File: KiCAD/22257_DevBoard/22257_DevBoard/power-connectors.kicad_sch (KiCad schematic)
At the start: 10 parts, among them U3 TPS73633DBV

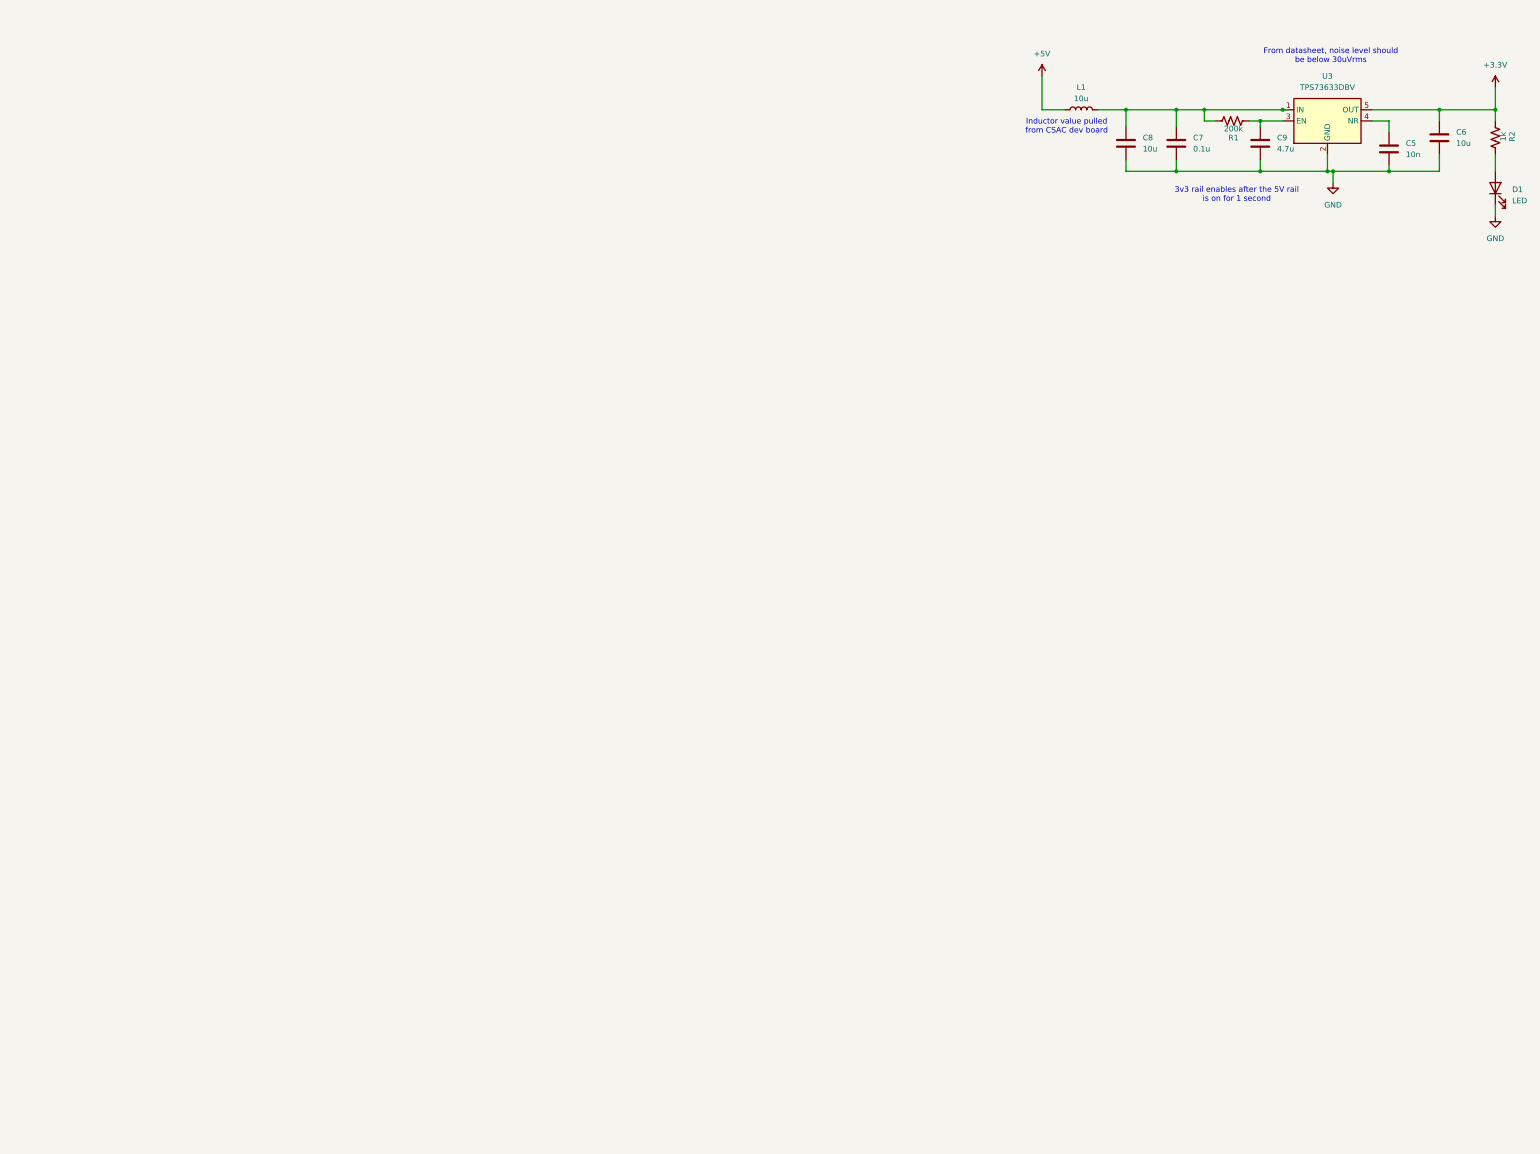
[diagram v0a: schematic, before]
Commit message: More Schematic Updates
Added power monitors and connectors, along with finishing the power circuitry.
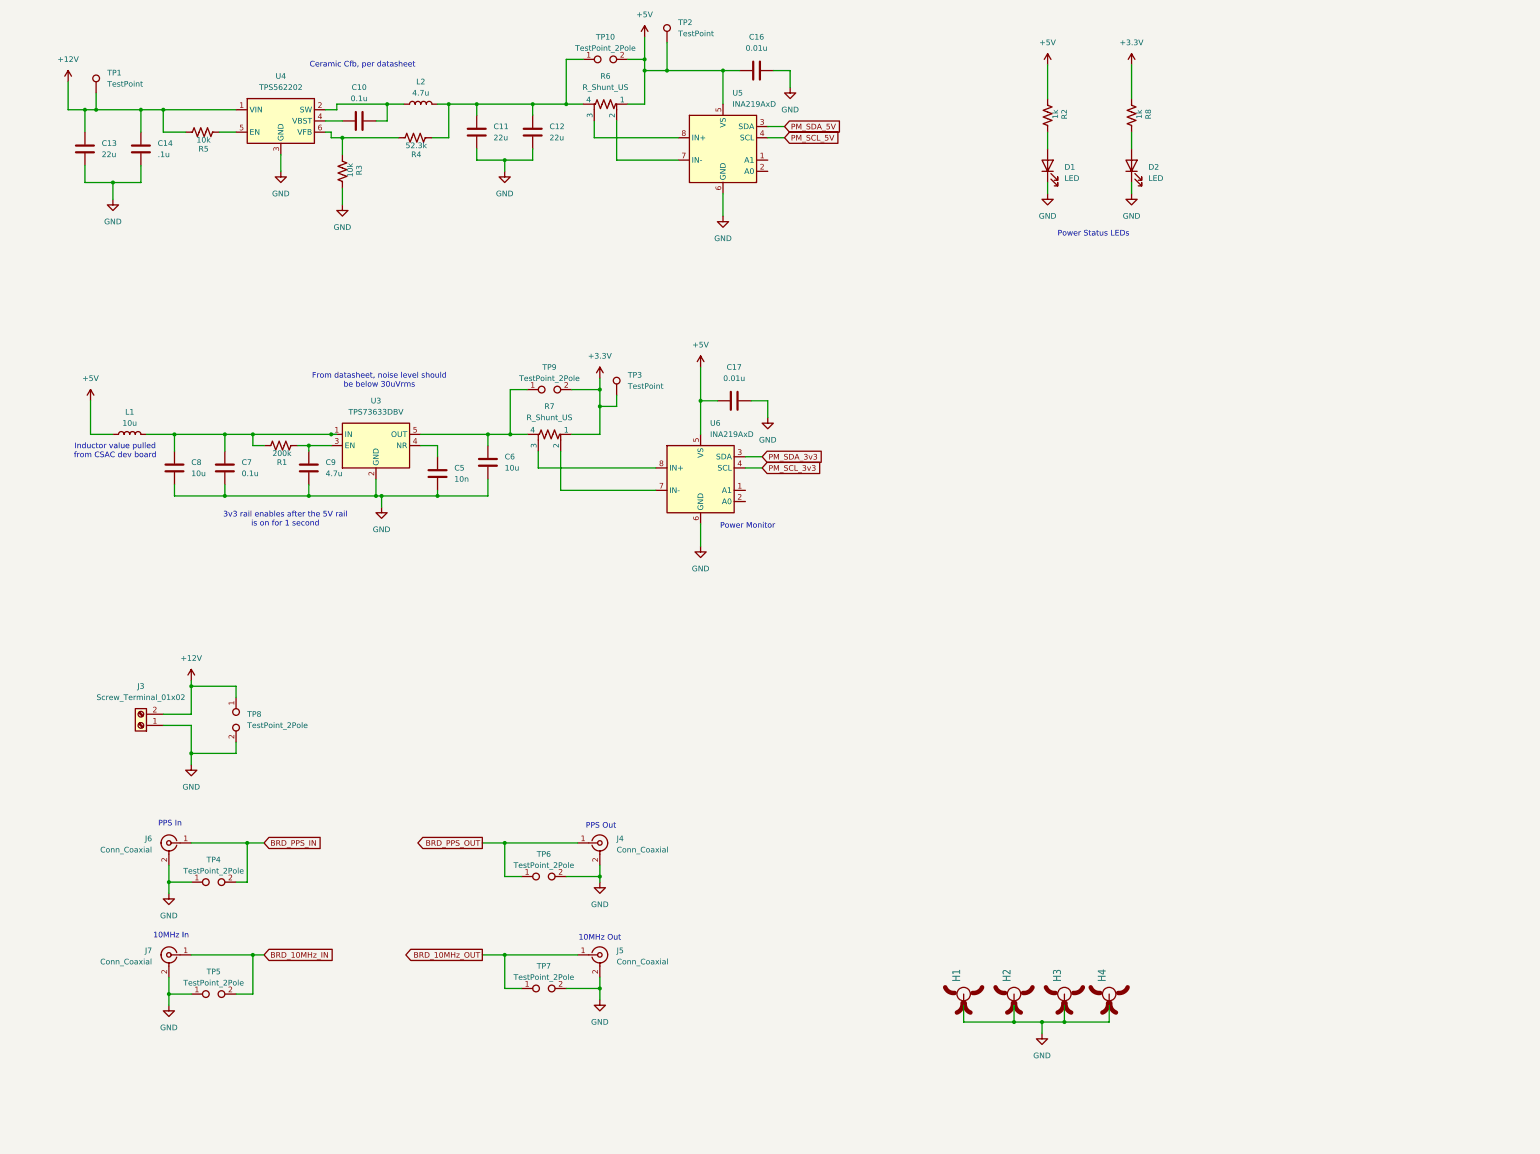
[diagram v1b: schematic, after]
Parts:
- added C10: 0.1u, symbol Device:C
- added C11, C12, C13: 22u, symbol Device:C
- added C14: .1u, symbol Device:C
- added C16, C17: 0.01u, symbol Device:C
- added D2: LED, symbol Device:LED
- added H1, H2, H3, H4: MOUNT-PAD-ROUND5.0, ZED_BREAKOUT_v22:5,0-PAD, symbol ZED_BREAKOUT_v22-eagle-import:MOUNT-PAD-ROUND5.0
- added J3: Screw_Terminal_01x02, symbol Connector:Screw_Terminal_01x02
- added J4, J5, J6, J7: Conn_Coaxial, symbol Connector:Conn_Coaxial
- added L2: 4.7u, symbol Device:L
- added R3, R5: 10k, symbol Device:R_US
- added R4: 52.3k, symbol Device:R_US
- added R6, R7: R_Shunt_US, symbol Device:R_Shunt_US
- added R8: 1k, symbol Device:R_US
- added TP1, TP2, TP3: TestPoint, symbol Connector:TestPoint
- added TP10, TP4, TP5, TP6, TP7, TP8, TP9: TestPoint_2Pole, symbol Connector:TestPoint_2Pole
- added U4: TPS562202, Package_TO_SOT_SMD:SOT-563, symbol Regulator_Switching:TPS562202
- added U5, U6: INA219AxD, Package_SO:SOIC-8_3.9x4.9mm_P1.27mm, symbol Sensor_Energy:INA219AxD
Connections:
- net +3.3V: now also R7.1, R8.2, TP3.1, TP9.2; no longer C6.1, R2.2, U3.5 (OUT)
- net +5V: now also R2.2, C16.1, C17.1, R6.1, TP10.2, TP2.1, U5.5 (VS), U6.5 (VS)
- net GND: now also C11.1, C12.1, C13.1, C14.1, C16.2, C17.2, D2.1 (K), H1.B5 (MOUNT), H2.B5 (MOUNT), H3.B5 (MOUNT), H4.B5 (MOUNT), J3.1 (Pin_1), J4.2 (Ext), J5.2 (Ext), J6.2 (Ext), J7.2 (Ext), R3.1, TP4.1, TP5.1, TP6.2, TP7.2, TP8.2, U4.3 (GND), U5.6 (GND), U6.6 (GND)
- new net: R7.2, U6.7 (IN-)
- new net: R7.3, U6.8 (IN+)
- new net: C6.1, R7.4, TP9.1, U3.5 (OUT)
- new net: R3.2, R4.1, U4.6 (VFB)
- new net: C11.2, C12.2, L2.2, R4.2, R6.4, TP10.1
- new net: R6.2, U5.7 (IN-)
- new net: R6.3, U5.8 (IN+)
- new net: C10.2, L2.1, U4.2 (SW)
- new net: C10.1, U4.4 (VBST)
- new net: R5.2, U4.5 (EN)
- new net: D2.2 (A), R8.1
- new net +12V: C13.2, C14.2, J3.2 (Pin_2), R5.1, TP1.1, TP8.1, U4.1 (VIN)
- new net BRD_10MHz_IN: J7.1 (In), TP5.2
- new net BRD_10MHz_OUT: J5.1 (In), TP7.1
- new net BRD_PPS_IN: J6.1 (In), TP4.2
- new net BRD_PPS_OUT: J4.1 (In), TP6.1
- new net PM_SCL_3v3: U6.4 (SCL)
- new net PM_SCL_5V: U5.4 (SCL)
- new net PM_SDA_3v3: U6.3 (SDA)
- new net PM_SDA_5V: U5.3 (SDA)
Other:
- note added: "10MHz In"
- note added: "10MHz Out"
- note added: "Ceramic Cfb, per datasheet"
- note added: "PPS In"
- note added: "PPS Out"
- note added: "Power Monitor"
- note added: "Power Status LEDs"
- moved on the sheet: C5, C6, C7, C8, C9, D1, L1, R1, R2, U3

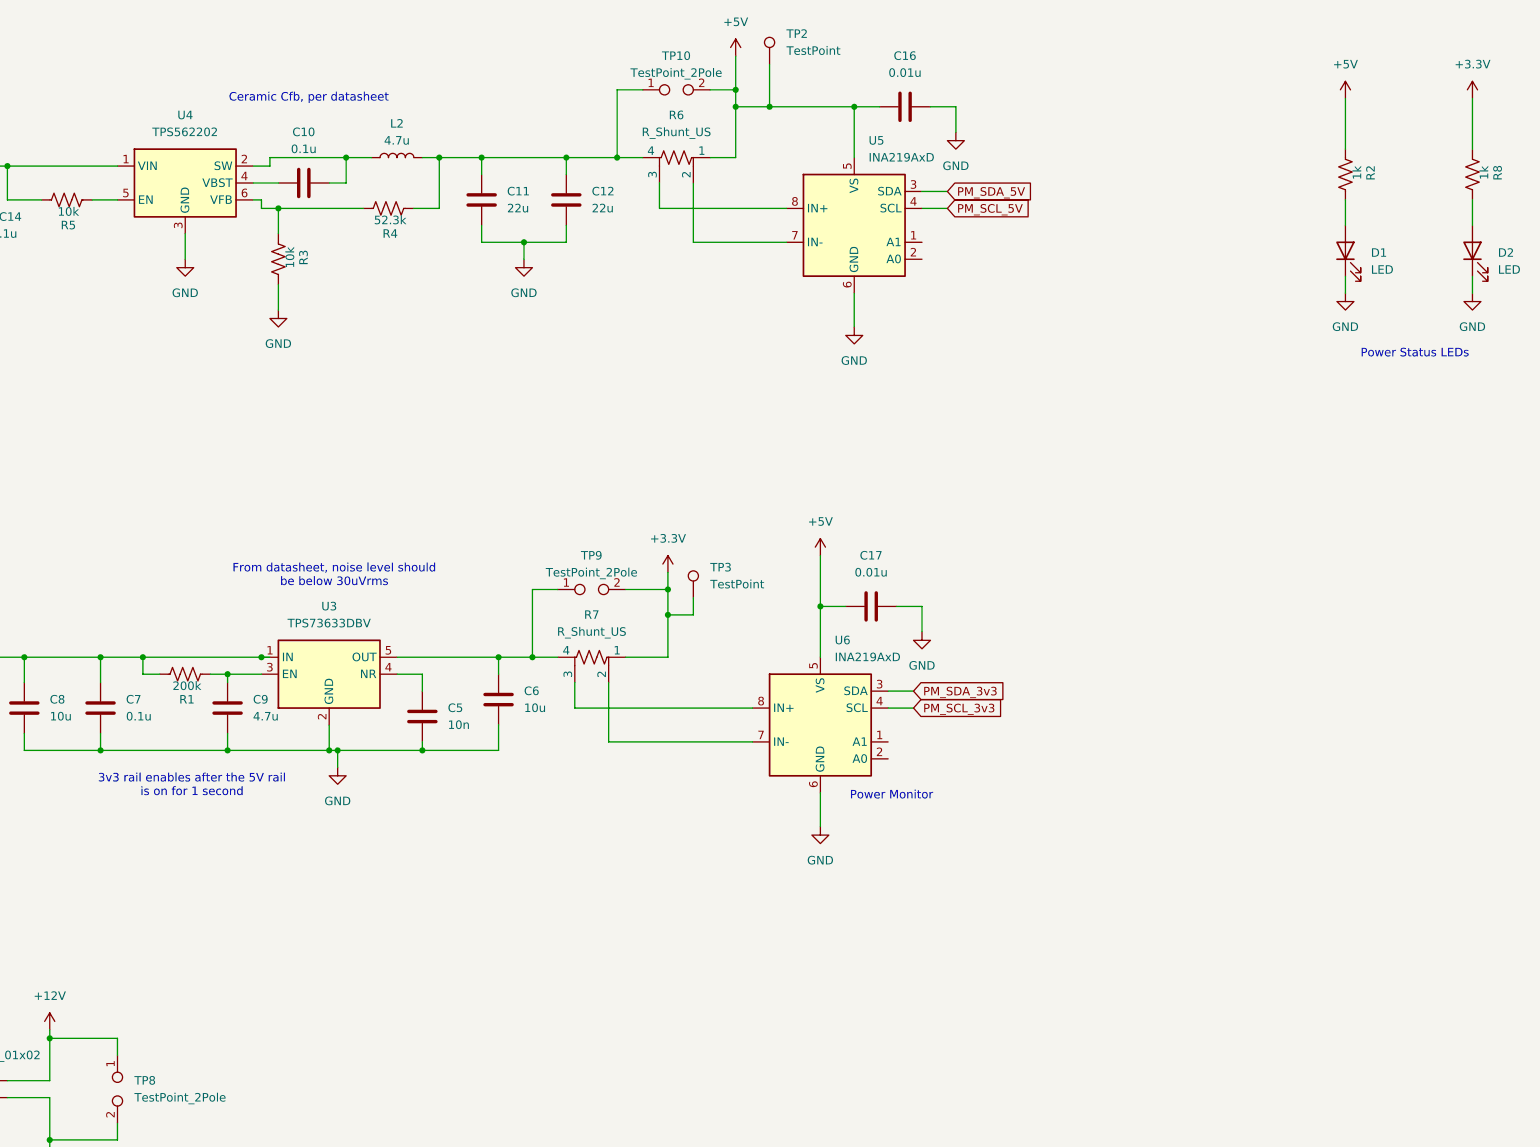
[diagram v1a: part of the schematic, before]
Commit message: Schematic should be finished, onto layout
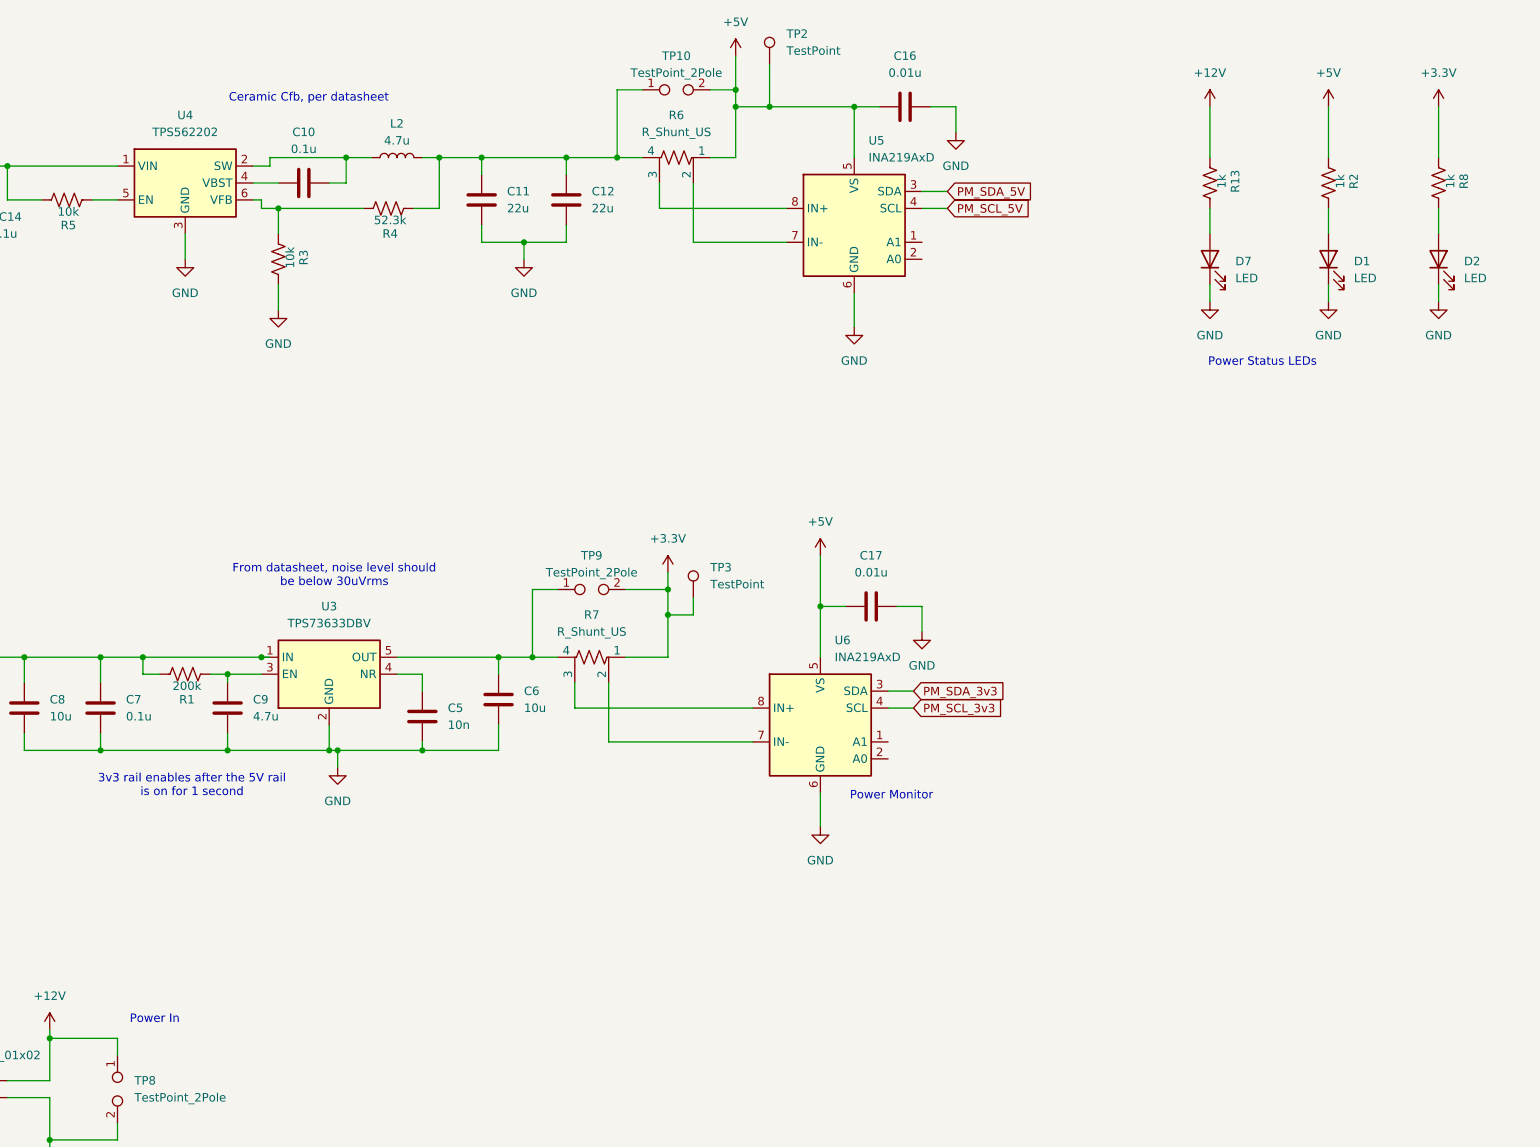
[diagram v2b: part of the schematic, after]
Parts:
- added D7: LED, symbol Device:LED
- added R13: 1k, symbol Device:R_US
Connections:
- net +12V: now also R13.2
- net GND: now also D7.1 (K)
- new net: D7.2 (A), R13.1
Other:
- note added: "Power In"
- moved on the sheet: D1, D2, R2, R8

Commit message: Assignmed Most footprints. Created footprints for oscillators.
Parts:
- C10, C11, C12, C13, C14, C16, C17, C5, C6, C7, C8, C9: footprint (none) -> Capacitor_SMD:C_0603_1608Metric
- D1, D2, D7: footprint (none) -> LED_SMD:LED_0603_1608Metric
- J3: footprint (none) -> Connector_Phoenix_GMSTB:PhoenixContact_GMSTBA_2,5_2-G-7,62_1x02_P7.62mm_Horizontal
- J4, J5, J6, J7: footprint (none) -> Connector_Coaxial:SMA_Amphenol_901-143_Horizontal
- R1, R2, R3, R4, R5: footprint (none) -> Resistor_SMD:R_0603_1608Metric
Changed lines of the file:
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@@
 			)
 		)
-		(property "Footprint" ""
+		(property "Footprint" "Capacitor_SMD:C_0603_1608Metric"
 			(at 120.3452 132.08 0)
 			(effects
@@
 			)
 		)
-		(property "Footprint" ""
+		(property "Footprint" "Capacitor_SMD:C_0603_1608Metric"
 			(at 190.5 110.7948 0)
 			(effects
@@
 			)
 		)
-		(property "Footprint" ""
+		(property "Footprint" "Capacitor_SMD:C_0603_1608Metric"
 			(at 195.58 35.8648 0)
 			(effects
@@
 			)
 		)
-		(property "Footprint" ""
+		(property "Footprint" "Resistor_SMD:R_0603_1608Metric"
 			(at 114.554 51.054 90)
 			(effects
@@
 			)
 		)
-		(property "Footprint" ""
+		(property "Footprint" "Resistor_SMD:R_0603_1608Metric"
 			(at 96.774 59.436 90)
 			(effects
@@
 			)
 		)
-		(property "Footprint" ""
+		(property "Footprint" "LED_SMD:LED_0603_1608Metric"
 			(at 255.27 59.69 0)
 			(effects
@@
 			)
 		)
-		(property "Footprint" ""
+		(property "Footprint" "Connector_Phoenix_GMSTB:PhoenixContact_GMSTBA_2,5_2-G-7,62_1x02_P7.62mm_Horizontal"
 			(at 52.07 185.42 0)
 			(effects
@@
 			)
 		)
-		(property "Footprint" ""
+		(property "Footprint" "Capacitor_SMD:C_0603_1608Metric"
 			(at 131.7752 129.54 0)
 			(effects
@@
 			)
 		)
-		(property "Footprint" ""
+		(property "Footprint" "Capacitor_SMD:C_0603_1608Metric"
 			(at 51.1048 50.8 0)
 			(effects
@@
 			)
 		)
-		(property "Footprint" ""
+		(property "Footprint" "Connector_Coaxial:SMA_Amphenol_901-143_Horizontal"
 			(at 156.21 212.09 0)
 			(effects
@@
 			)
 		)
-		(property "Footprint" ""
+		(property "Footprint" "LED_SMD:LED_0603_1608Metric"
 			(at 237.49 59.69 0)
 			(effects
@@
 			)
 		)
-		(property "Footprint" ""
+		(property "Footprint" "Capacitor_SMD:C_0603_1608Metric"
 			(at 60.6552 130.81 0)
 			(effects
@@
 			)
 		)
-		(property "Footprint" ""
+		(property "Footprint" "Resistor_SMD:R_0603_1608Metric"
 			(at 66.294 49.784 90)
 			(effects
@@
 			)
 		)
-		(property "Footprint" ""
+		(property "Footprint" "LED_SMD:LED_0603_1608Metric"
 			(at 271.78 59.69 0)
 			(effects
@@
 			)
 		)
-		(property "Footprint" ""
+		(property "Footprint" "Resistor_SMD:R_0603_1608Metric"
 			(at 254.254 48.006 90)
 			(effects
@@
 			)
 		)
-		(property "Footprint" ""
+		(property "Footprint" "Connector_Coaxial:SMA_Amphenol_901-143_Horizontal"
 			(at 58.42 237.49 0)
 			(effects
@@
 			)
 		)
-		(property "Footprint" ""
+		(property "Footprint" "Capacitor_SMD:C_0603_1608Metric"
 			(at 127.3048 46.99 0)
 			(effects
@@
 			)
 		)
-		(property "Footprint" ""
+		(property "Footprint" "Capacitor_SMD:C_0603_1608Metric"
 			(at 38.4048 50.8 0)
 			(effects
@@
 			)
 		)
-		(property "Footprint" ""
+		(property "Footprint" "Capacitor_SMD:C_0603_1608Metric"
 			(at 72.0852 130.81 0)
 			(effects
@@
 			)
 		)
-		(property "Footprint" ""
+		(property "Footprint" "Capacitor_SMD:C_0603_1608Metric"
 			(at 105.41 47.2948 0)
 			(effects
@@
 			)
 		)
-		(property "Footprint" ""
+		(property "Footprint" "Connector_Coaxial:SMA_Amphenol_901-143_Horizontal"
 			(at 58.42 212.09 0)
 			(effects
@@
 			)
 		)
-		(property "Footprint" ""
+		(property "Footprint" "Capacitor_SMD:C_0603_1608Metric"
 			(at 91.1352 130.81 0)
 			(effects
@@
 			)
 		)
-		(property "Footprint" ""
+		(property "Footprint" "Connector_Coaxial:SMA_Amphenol_901-143_Horizontal"
 			(at 156.21 237.49 0)
 			(effects
@@
 			)
 		)
-		(property "Footprint" ""
+		(property "Footprint" "Resistor_SMD:R_0603_1608Metric"
 			(at 84.074 120.904 90)
 			(effects
@@
 			)
 		)
-		(property "Footprint" ""
+		(property "Footprint" "Capacitor_SMD:C_0603_1608Metric"
 			(at 140.0048 46.99 0)
 			(effects
